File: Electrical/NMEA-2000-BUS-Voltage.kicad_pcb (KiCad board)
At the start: 2 copper layers, 52.1 x 40.6 mm, 12 parts, among them J1 Conn_01x06, SW1 SW_Push, U1 WeMos_D1_mini, U2 LM7805_TO220

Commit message: Updated PCB
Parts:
- added C10: 1uF, Capacitor_THT:C_Disc_D5.0mm_W2.5mm_P5.00mm, F.Cu at (139.2, 85.4)
- added C11: 0.33uF, Capacitor_THT:C_Disc_D5.0mm_W2.5mm_P5.00mm, F.Cu at (112.0, 75.4)
- added C12: 20pF, Capacitor_THT:C_Disc_D5.0mm_W2.5mm_P5.00mm, F.Cu at (137.4, 70.9)
- added C13: 0.1uF, Capacitor_THT:C_Disc_D5.0mm_W2.5mm_P5.00mm, F.Cu at (139.2, 94.7)
- added C14: 0.1uF, Capacitor_THT:C_Disc_D5.0mm_W2.5mm_P5.00mm, F.Cu at (152.7, 53.6)
- added C15: 20pF, Capacitor_THT:C_Disc_D5.0mm_W2.5mm_P5.00mm, F.Cu at (143.8, 70.9)
- added C16: 0.1uF, Capacitor_THT:C_Disc_D5.0mm_W2.5mm_P5.00mm, F.Cu at (119.4, 72.3)
- added C17: 0.1uF, Capacitor_THT:C_Disc_D5.0mm_W2.5mm_P5.00mm, F.Cu at (166.9, 65.0)
- added C18: 0.1nF, Capacitor_THT:C_Disc_D5.0mm_W2.5mm_P5.00mm, F.Cu at (183.6, 71.6)
- added C19: 0.1uF, Capacitor_THT:C_Disc_D5.0mm_W2.5mm_P5.00mm, F.Cu at (162.0, 59.1)
- added C20: 0.1uF, Capacitor_THT:C_Disc_D5.0mm_W2.5mm_P5.00mm, F.Cu at (150.1, 64.8)
- added C21: 10nF, Capacitor_THT:C_Disc_D5.0mm_W2.5mm_P5.00mm, F.Cu at (95.9, 109.9)
- added C22: 10nF, Capacitor_THT:C_Disc_D5.0mm_W2.5mm_P5.00mm, F.Cu at (180.4, 109.9)
- added C23: 0.1uF, Capacitor_THT:C_Disc_D5.0mm_W2.5mm_P5.00mm, F.Cu at (96.1, 114.0)
- added C24: 10nF, Capacitor_THT:C_Disc_D5.0mm_W2.5mm_P5.00mm, F.Cu at (104.8, 114.3)
- added C25: 0.1uF, Capacitor_THT:C_Disc_D5.0mm_W2.5mm_P5.00mm, F.Cu at (180.3, 113.7)
- added C26: 10nF, Capacitor_THT:C_Disc_D5.0mm_W2.5mm_P5.00mm, F.Cu at (189.2, 114.3)
- added C27: 1uF, Capacitor_THT:C_Disc_D5.0mm_W2.5mm_P5.00mm, F.Cu at (191.8, 104.1)
- added C28: 0.1uF, Capacitor_THT:C_Disc_D5.0mm_W2.5mm_P5.00mm, F.Cu at (191.8, 98.8)
- added C29: 220nF, Capacitor_THT:C_Disc_D5.0mm_W2.5mm_P5.00mm, F.Cu at (149.4, 101.1)
- added C30: 0.1uF, Capacitor_THT:C_Disc_D5.0mm_W2.5mm_P5.00mm, F.Cu at (188.3, 91.7)
- added C4: 0.33uF, Capacitor_THT:C_Disc_D5.0mm_W2.5mm_P5.00mm, F.Cu at (90.9, 86.4)
- added C5: 0.1uF, Capacitor_THT:C_Disc_D5.0mm_W2.5mm_P5.00mm, F.Cu at (141.7, 43.7)
- added C6: 0.1uF, Capacitor_THT:C_Disc_D5.0mm_W2.5mm_P5.00mm, F.Cu at (122.9, 85.5)
- added C7: 20pF, Capacitor_THT:C_Disc_D5.0mm_W2.5mm_P5.00mm, F.Cu at (161.0, 79.0)
- added C8: 10nF, Capacitor_THT:C_Disc_D5.0mm_W2.5mm_P5.00mm, F.Cu at (132.8, 85.3)
- added C9: 0.1uF, Capacitor_THT:C_Disc_D5.0mm_W2.5mm_P5.00mm, F.Cu at (105.2, 86.4)
- added D2: LED, LED_THT:LED_D5.0mm, F.Cu at (81.9, 44.5)
- added D3: LED, LED_THT:LED_D5.0mm, F.Cu at (89.5, 44.4)
- added D4: LED, LED_THT:LED_D5.0mm, F.Cu at (97.2, 44.5)
- added D5: LED, LED_THT:LED_D5.0mm, F.Cu at (104.8, 44.5)
- added D6: 1N5819, Diode_THT:D_DO-41_SOD81_P10.16mm_Horizontal, F.Cu at (217.2, 83.6)
- added D7: 1N5819, Diode_THT:D_DO-41_SOD81_P10.16mm_Horizontal, F.Cu at (216.9, 109.5)
- added F1: Polyfuse, Diode_SMD:D_1210_3225Metric_Pad1.42x2.65mm_HandSolder, F.Cu at (82.0, 87.4)
- added H1: MountingHole_Pad, MountingHole:MountingHole_6mm_Pad, F.Cu at (68.6, 50.8)
- added H2: MountingHole_Pad, MountingHole:MountingHole_6mm_Pad, F.Cu at (228.6, 50.8)
- added H3: MountingHole_Pad, MountingHole:MountingHole_6mm_Pad, F.Cu at (68.6, 130.8)
- added H4: MountingHole_Pad, MountingHole:MountingHole_6mm_Pad, F.Cu at (228.6, 130.8)
- added IC1: ADS131M08, ADS131M08QPBSRQ1:QFP50P700X700X120-32N, F.Cu at (139.2, 106.8)
- added J10: Conn_01x02, TerminalBlock_Phoenix:TerminalBlock_Phoenix_PT-1,5-2-5.0-H_1x02_P5.00mm_Horizontal, F.Cu at (166.4, 135.4)
- added J11: Conn_01x05, Connector_PinHeader_2.54mm:PinHeader_1x05_P2.54mm_Vertical, F.Cu at (143.3, 135.6)
- added J12: Conn_01x02, TerminalBlock_Phoenix:TerminalBlock_Phoenix_PT-1,5-2-5.0-H_1x02_P5.00mm_Horizontal, F.Cu at (233.2, 83.2)
- added J13: Conn_01x02, TerminalBlock_Phoenix:TerminalBlock_Phoenix_PT-1,5-2-5.0-H_1x02_P5.00mm_Horizontal, F.Cu at (233.3, 107.7)
- added J2: Conn_01x04, Connector_PinSocket_2.54mm:PinSocket_1x04_P2.54mm_Horizontal, F.Cu at (171.2, 51.6)
- added J3: Conn_02x08_Counter_Clockwise, Connector_PinHeader_2.54mm:PinHeader_2x09_P2.54mm_Vertical, F.Cu at (186.7, 51.1)
- added J4: Conn_01x04, Connector:FanPinHeader_1x04_P2.54mm_Vertical, F.Cu at (194.3, 62.7)
- added J5: Conn_01x05, TerminalBlock_Phoenix:TerminalBlock_Phoenix_PT-1,5-5-5.0-H_1x05_P5.00mm_Horizontal, F.Cu at (109.0, 135.5)
- added J6: Conn_01x05, TerminalBlock_Phoenix:TerminalBlock_Phoenix_PT-1,5-5-5.0-H_1x05_P5.00mm_Horizontal, F.Cu at (194.6, 135.4)
- added J7: Conn_01x02, TerminalBlock_Phoenix:TerminalBlock_Phoenix_PT-1,5-2-5.0-H_1x02_P5.00mm_Horizontal, F.Cu at (83.6, 135.5)
- added J8: Conn_01x02, TerminalBlock_Phoenix:TerminalBlock_Phoenix_PT-1,5-2-5.0-H_1x02_P5.00mm_Horizontal, F.Cu at (96.1, 135.5)
- added J9: Conn_01x02, TerminalBlock_Phoenix:TerminalBlock_Phoenix_PT-1,5-2-5.0-H_1x02_P5.00mm_Horizontal, F.Cu at (180.3, 135.4)
- added JP1: Jumper_2_Open, Connector_PinHeader_2.54mm:PinHeader_1x02_P2.54mm_Vertical, F.Cu at (80.8, 81.5)
- added JP2: Jumper_3_Bridged12, Connector_PinHeader_2.54mm:PinHeader_1x03_P2.54mm_Vertical, F.Cu at (100.1, 103.1)
- added JP3: Jumper_3_Bridged12, Connector_PinHeader_2.54mm:PinHeader_1x03_P2.54mm_Vertical, F.Cu at (107.7, 103.1)
- added JP4: Jumper_2_Open, Connector_PinHeader_2.54mm:PinHeader_1x02_P2.54mm_Vertical, F.Cu at (80.5, 94.5)
- added JP5: Jumper_3_Bridged12, Connector_PinHeader_2.54mm:PinHeader_1x03_P2.54mm_Vertical, F.Cu at (186.4, 99.1)
- added JP6: Jumper_3_Bridged12, Connector_PinHeader_2.54mm:PinHeader_1x03_P2.54mm_Vertical, F.Cu at (221.2, 71.6)
- added JP7: Jumper_3_Bridged12, Connector_PinHeader_2.54mm:PinHeader_1x03_P2.54mm_Vertical, F.Cu at (220.2, 97.8)
- added JP8: Jumper_2_Bridged, Connector_PinHeader_2.54mm:PinHeader_1x02_P2.54mm_Vertical, F.Cu at (222.0, 81.0)
- added JP9: Jumper_2_Bridged, Connector_PinHeader_2.54mm:PinHeader_1x02_P2.54mm_Vertical, F.Cu at (223.3, 103.6)
- added L1: CBG322513U102T, Inductor_SMD:L_1210_3225Metric_Pad1.42x2.65mm_HandSolder, F.Cu at (128.0, 85.3)
- added Q1: IRFZ44N, Package_TO_SOT_THT:TO-220-3_Vertical, F.Cu at (207.0, 78.0)
- added Q2: IRFZ44N, Package_TO_SOT_THT:TO-220-3_Vertical, F.Cu at (206.8, 102.9)
- added R10: 10k, Resistor_THT:R_Axial_DIN0207_L6.3mm_D2.5mm_P10.16mm_Horizontal, F.Cu at (178.6, 60.7)
- added R11: 3.3k, Resistor_THT:R_Axial_DIN0207_L6.3mm_D2.5mm_P10.16mm_Horizontal, F.Cu at (188.7, 67.3)
- added R12: 10k, Resistor_THT:R_Axial_DIN0207_L6.3mm_D2.5mm_P10.16mm_Horizontal, F.Cu at (83.6, 128.8)
- added R13: 4k7, Resistor_THT:R_Axial_DIN0207_L6.3mm_D2.5mm_P10.16mm_Horizontal, F.Cu at (88.6, 118.6)
- added R14: 10k, Resistor_THT:R_Axial_DIN0207_L6.3mm_D2.5mm_P10.16mm_Horizontal, F.Cu at (128.9, 128.9)
- added R15: 10k, Resistor_THT:R_Axial_DIN0207_L6.3mm_D2.5mm_P10.16mm_Horizontal, F.Cu at (204.5, 128.3)
- added R16: 10k, Resistor_THT:R_Axial_DIN0207_L6.3mm_D2.5mm_P10.16mm_Horizontal, F.Cu at (166.4, 128.8)
- added R17: 4k7, Resistor_THT:R_Axial_DIN0207_L6.3mm_D2.5mm_P10.16mm_Horizontal, F.Cu at (171.4, 118.6)
- added R18: 10k, Resistor_THT:R_Axial_DIN0207_L6.3mm_D2.5mm_P10.16mm_Horizontal, F.Cu at (104.9, 128.8)
- added R19: 10k, Resistor_THT:R_Axial_DIN0207_L6.3mm_D2.5mm_P10.16mm_Horizontal, F.Cu at (189.2, 128.3)
- added R20: 1k, Resistor_THT:R_Axial_DIN0207_L6.3mm_D2.5mm_P10.16mm_Horizontal, F.Cu at (96.0, 128.8)
- added R21: 1k, Resistor_THT:R_Axial_DIN0207_L6.3mm_D2.5mm_P10.16mm_Horizontal, F.Cu at (100.3, 128.8)
- added R22: 1k, Resistor_THT:R_Axial_DIN0207_L6.3mm_D2.5mm_P10.16mm_Horizontal, F.Cu at (180.3, 128.3)
- added R23: 1k, Resistor_THT:R_Axial_DIN0207_L6.3mm_D2.5mm_P10.16mm_Horizontal, F.Cu at (184.8, 128.3)
- added R24: 120R, Resistor_THT:R_Axial_DIN0207_L6.3mm_D2.5mm_P10.16mm_Horizontal, F.Cu at (209.6, 61.0)
- added R25: 120R, Resistor_THT:R_Axial_DIN0207_L6.3mm_D2.5mm_P10.16mm_Horizontal, F.Cu at (219.5, 91.4)
- added R26: 10k, Resistor_THT:R_Axial_DIN0207_L6.3mm_D2.5mm_P10.16mm_Horizontal, F.Cu at (216.5, 62.2)
- added R27: 10k, Resistor_THT:R_Axial_DIN0207_L6.3mm_D2.5mm_P10.16mm_Horizontal, F.Cu at (224.2, 91.4)
- added R5: 470R, Resistor_THT:R_Axial_DIN0207_L6.3mm_D2.5mm_P10.16mm_Horizontal, F.Cu at (89.5, 61.6)
- added R6: 10k, Resistor_THT:R_Axial_DIN0207_L6.3mm_D2.5mm_P10.16mm_Horizontal, F.Cu at (116.6, 105.7)
- added R7: 330R, Resistor_THT:R_Axial_DIN0207_L6.3mm_D2.5mm_P10.16mm_Horizontal, F.Cu at (97.2, 61.6)
- added R8: 1k5, Resistor_THT:R_Axial_DIN0207_L6.3mm_D2.5mm_P10.16mm_Horizontal, F.Cu at (104.8, 61.6)
- added R9: 120R, Resistor_THT:R_Axial_DIN0207_L6.3mm_D2.5mm_P10.16mm_Horizontal, F.Cu at (87.4, 108.5)
- added SW2: SW_Push, Button_Switch_THT:SW_PUSH_6mm, F.Cu at (147.3, 43.9)
- added TP1: 12V, TestPoint:TestPoint_Pad_3.0x3.0mm, F.Cu at (81.9, 66.0)
- added TP2: 5V, TestPoint:TestPoint_Pad_3.0x3.0mm, F.Cu at (89.5, 66.0)
- added TP3: 3.3V, TestPoint:TestPoint_Pad_3.0x3.0mm, F.Cu at (97.2, 66.0)
- added TP4: VMot, TestPoint:TestPoint_Pad_3.0x3.0mm, F.Cu at (104.8, 66.0)
- added U3: STM32G431CBTx, Package_QFP:LQFP-48_7x7mm_P0.5mm, F.Cu at (173.5, 83.4)
- added U4: SN65HVD230, Package_SO:SOIC-8_3.9x4.9mm_P1.27mm, F.Cu at (91.1, 94.9)
- added U5: BMP280, N2K-influx:Bosch_LGA-8_2x2.5mm_P0.65mm_ClockwisePinNumbering, F.Cu at (157.7, 63.7)
- added U6: ADR4533, Package_SO:SOIC-8_3.9x4.9mm_P1.27mm, F.Cu at (177.3, 102.1)
- added Y1: K7A080002020, Crystal:Crystal_SMD_7050-4Pin_7.0x5.0mm, F.Cu at (153.7, 81.8)
- added Y2: X308032768KGB2SC, Crystal:Crystal_C38-LF_D3.0mm_L8.0mm_Horizontal, F.Cu at (149.9, 75.6)
- added Y3: 20kHz Crystal, Crystal:Crystal_AT310_D3.0mm_L10.0mm_Horizontal, F.Cu at (167.1, 102.6)
- C1: value 0.2uF -> 0.1uF; footprint Capacitor_THT:CP_Radial_D4.0mm_P1.50mm -> Capacitor_THT:C_Disc_D5.0mm_W2.5mm_P5.00mm
- C2: footprint Capacitor_THT:CP_Radial_D4.0mm_P1.50mm -> Capacitor_THT:C_Disc_D5.0mm_W2.5mm_P5.00mm
- C3: value 0.1uF -> 20pF; footprint Capacitor_THT:CP_Radial_D4.0mm_P1.50mm -> Capacitor_THT:C_Disc_D5.0mm_W2.5mm_P5.00mm
- D1: value LED -> 1N5819; footprint LED_THT:LED_D1.8mm_W3.3mm_H2.4mm -> Diode_THT:D_DO-41_SOD81_P10.16mm_Horizontal
- J1: value Conn_01x06 -> Conn_01x04; footprint Connector_PinHeader_2.00mm:PinHeader_1x06_P2.00mm_Horizontal -> TerminalBlock_Phoenix:TerminalBlock_Phoenix_PT-1,5-4-5.0-H_1x04_P5.00mm_Horizontal
- R1: footprint Resistor_THT:R_Axial_DIN0204_L3.6mm_D1.6mm_P5.08mm_Horizontal -> Resistor_THT:R_Axial_DIN0207_L6.3mm_D2.5mm_P10.16mm_Horizontal
- R2: value 20k -> 0R; footprint Resistor_THT:R_Axial_DIN0204_L3.6mm_D1.6mm_P5.08mm_Horizontal -> Resistor_THT:R_Axial_DIN0207_L6.3mm_D2.5mm_P10.16mm_Horizontal
- R3: value 120k -> 10k; footprint Resistor_THT:R_Axial_DIN0204_L3.6mm_D1.6mm_P5.08mm_Horizontal -> Resistor_THT:R_Axial_DIN0207_L6.3mm_D2.5mm_P10.16mm_Horizontal
- R4: value 1k -> 1.2k; footprint Resistor_THT:R_Axial_DIN0204_L3.6mm_D1.6mm_P5.08mm_Horizontal -> Resistor_THT:R_Axial_DIN0207_L6.3mm_D2.5mm_P10.16mm_Horizontal
- SW1: footprint Button_Switch_THT:SW_TH_Tactile_Omron_B3F-10xx -> Button_Switch_THT:SW_PUSH_6mm
- U1: value WeMos_D1_mini -> LM7805_TO220; footprint Module:WEMOS_D1_mini_light -> Package_TO_SOT_THT:TO-220-3_Vertical
- U2: value LM7805_TO220 -> AMS1117-3.3; footprint Package_TO_SOT_THT:TO-220-3_Vertical -> Package_TO_SOT_SMD:SOT-223-3_TabPin2
- moved D1 103.4 mm to (166.9, 71.9), turned to 0 degrees
- moved R3 84.8 mm to (159.8, 68.8), turned to 180 degrees
- moved C3 76.1 mm to (150.9, 87.6), turned to 0 degrees
- moved SW1 70.0 mm to (126.2, 44.2)
- moved R2 68.4 mm to (143.8, 80.3)
- moved R1 58.1 mm to (136.7, 53.6), turned to 0 degrees
- moved U2 48.2 mm to (128.7, 74.9), turned to 0 degrees
- moved C2 41.5 mm to (109.7, 85.5), turned to -90 degrees
- moved C1 36.0 mm to (116.3, 85.4), turned to -90 degrees
- moved J1 23.7 mm to (63.9, 83.9), turned to -90 degrees
- moved U1 21.4 mm to (95.8, 79.8)
- moved R4 17.3 mm to (81.9, 61.6)
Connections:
- C1 pad 1: +12V -> +3.3V
- C1 pad 2: Net-(C1-Pad2) -> GND
- C2 pad 1: +5V -> +3.3V
- C3 pad 1: Net-(C1-Pad2) -> Net-(U3-PF1)
- D1 pad 2: +5V -> +3.3V
- J1 pad 1: +12V -> VMot
- J1 pad 2: /D4 -> /CAN_L
- J1 pad 3: /RX -> /CAN_H
- J1 pad 4: /TX -> GND
- R1 pad 1: +12V -> GND
- R1 pad 2: /A0 -> Net-(U3-PB8)
- R2 pad 1: /A0 -> +3.3VA
- R2 pad 2: Net-(R2-Pad2) -> /V_{ref}+
- R3 pad 1: Net-(R2-Pad2) -> /EN
- R3 pad 2: GND -> +3.3V
- R4 pad 1: Net-(D1-K) -> +12V
- R4 pad 2: GND -> Net-(D2-A)
- SW1 pad 1: /FLASH -> +3.3V
- SW1 pad 2: GND -> Net-(U3-PB8)
- U1 pad 1: unconnected-(U1-~{RST}-Pad1) -> +12V
- U1 pad 2: /A0 -> GND
- U1 pad 3: unconnected-(U1-D0-Pad3) -> +5V
- U2 pad 1: +12V -> GND
- U2 pad 2: GND -> +3.3V
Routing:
- net +5V: track 60.7 -> 292.3 mm
- net +12V: track 33.6 -> 259.5 mm
- net /Sensor/V_{ref}: track 0.00 -> 154.8 mm
- net /CAN_{RX}: track 0.00 -> 122.6 mm, vias 0 -> 2
- net /CAN_{TX}: track 0.00 -> 114.9 mm, vias 0 -> 2
- net /PB14: track 0.00 -> 92.9 mm, vias 0 -> 2
- net /TX: track 38.7 -> 128.0 mm, vias 0 -> 1
- net /Sensor/AIN5P: track 0.00 -> 88.2 mm, vias 0 -> 1
- net +3.3V: track 0.00 -> 87.3 mm, vias 0 -> 3
- net /EN: track 0.00 -> 85.0 mm, vias 0 -> 1
- net REL2: track 0.00 -> 83.4 mm, vias 0 -> 1
- net REL1: track 0.00 -> 81.7 mm, vias 0 -> 1
- net /PB12: track 0.00 -> 80.4 mm, vias 0 -> 1
- net Net-(U3-PB8): track 0.00 -> 79.9 mm, vias 0 -> 2
- net /Sensor/AIN5N: track 0.00 -> 79.0 mm, vias 0 -> 1
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- added copper zone on F.Cu, net +3.3V
- added copper zone on B.Cu, net GND
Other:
- board size 52.1 x 40.6 mm -> 180.3 x 100.3 mm
- copper layers 2 -> 4
- board text removed: "12 D4 RX TX G G"
- board text removed: "Flash Mode"

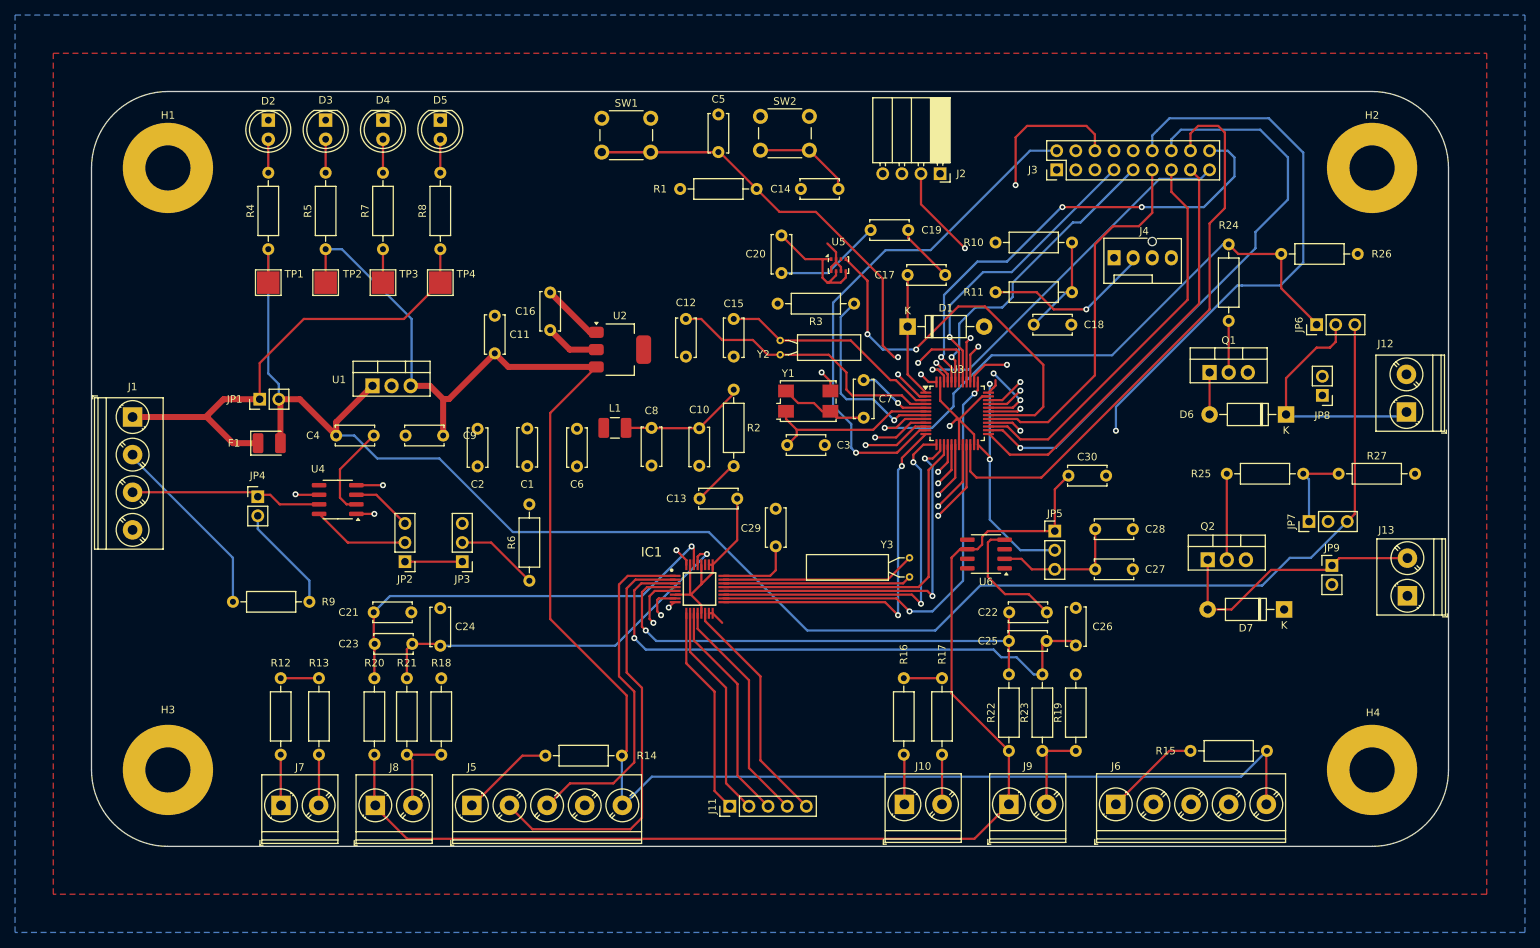
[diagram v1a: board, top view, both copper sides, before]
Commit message: Replaced SN65HVD230 with MCP2562
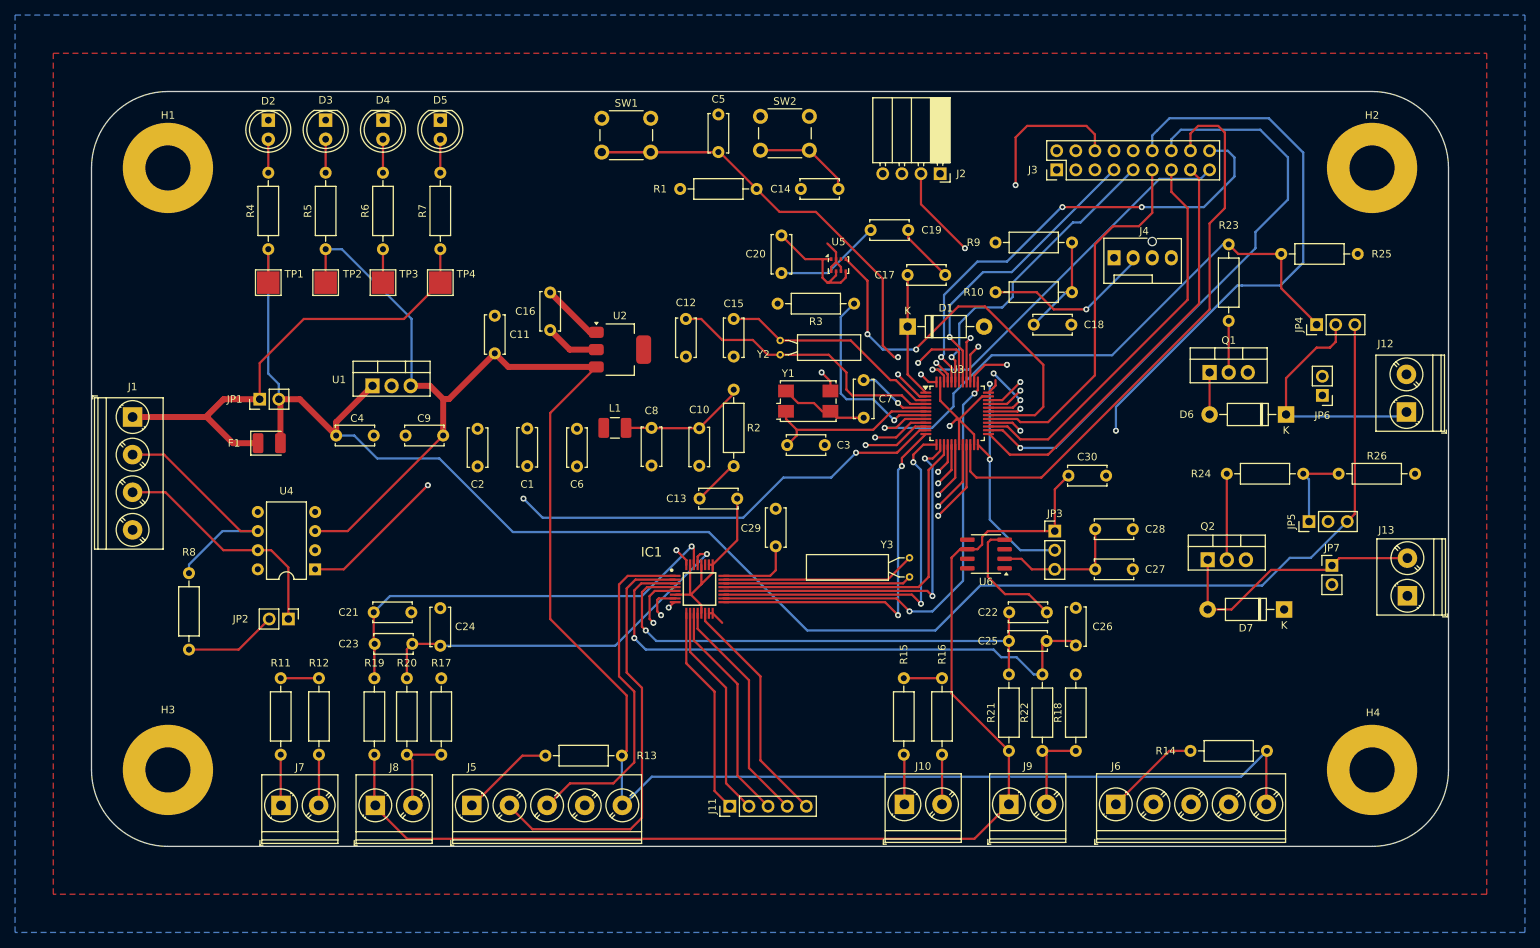
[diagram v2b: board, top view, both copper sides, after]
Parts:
- removed the JP3 at (107.7, 103.1)
- removed the JP4 at (80.5, 94.5)
- removed the R6 at (116.6, 105.7)
- removed the R9 at (87.4, 108.5)
- added R8: 120R, Resistor_THT:R_Axial_DIN0207_L6.3mm_D2.5mm_P10.16mm_Horizontal, F.Cu at (71.4, 114.8)
- JP2: value Jumper_3_Bridged12 -> Jumper_2_Open; footprint Connector_PinHeader_2.54mm:PinHeader_1x03_P2.54mm_Vertical -> Connector_PinHeader_2.54mm:PinHeader_1x02_P2.54mm_Vertical
- U4: value SN65HVD230 -> MCP2562-E-P; footprint Package_SO:SOIC-8_3.9x4.9mm_P1.27mm -> Package_DIP:DIP-8_W7.62mm
- moved JP2 17.3 mm to (84.6, 110.7), turned to -90 degrees
- moved U4 9.75 mm to (88.1, 104.1)
- renumbered JP5 to JP3, JP6 to JP4, JP7 to JP5, JP8 to JP6, JP9 to JP7, R11 to R10, R12 to R11, R13 to R12, R14 to R13, R15 to R14, R16 to R15, R17 to R16, R18 to R17, R19 to R18, R20 to R19, R21 to R20, R22 to R21, R23 to R22, R24 to R23, R25 to R24, R26 to R25, R27 to R26, R7 to R6, R8 to R7, R10 to R9
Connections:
- J3 pad 2: /PA3 -> unconnected-(J3-Pin_2-Pad2)
- JP2 pad 1: Net-(JP2-A) -> /CAN_H
- JP2 pad 2: Net-(JP2-C) -> Net-(JP2-B)
- U3 pad 11: /PA3 -> /STBY
- U4 pad 1: /CAN_{RX} -> /CAN_{TX}
- U4 pad 3: +3.3V -> +5V
- U4 pad 4: /CAN_{TX} -> /CAN_{RX}
- U4 pad 5: unconnected-(U4-Vref-Pad5) -> +3.3V
- U4 pad 8: Net-(JP2-C) -> /STBY
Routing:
- net /STBY: track 0.00 -> 100.6 mm, vias 0 -> 2
- net /PA3: track 69.8 -> 0.00 mm, vias 1 -> 0
- net +5V: track 292.3 -> 314.6 mm
- net Net-(JP4-B): track 14.3 -> 0.00 mm
- net Net-(JP2-C): track 13.0 -> 0.00 mm
- net GND: track 142.2 -> 129.5 mm
- net /CAN_L: track 46.0 -> 33.3 mm, vias 1 -> 0
- net Net-(JP2-B): track 0.00 -> 12.4 mm
- net Net-(JP3-C): track 11.0 -> 0.00 mm
- net /CAN_{TX}: track 114.9 -> 125.0 mm
- net +3.3V: track 87.3 -> 79.2 mm
- net Net-(JP2-A): track 7.62 -> 0.00 mm
- net /CAN_H: track 25.7 -> 31.7 mm
- net /CAN_{RX}: track 122.6 -> 126.6 mm, vias 2 -> 1
